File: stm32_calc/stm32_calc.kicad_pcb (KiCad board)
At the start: 2 copper layers, 76.2 x 132.2 mm, 83 parts, among them IC1 TM1638, J2 Conn_01x03, J3 C5307759, J4 Conn_02x03_Odd_Even, Q1 p channel mosfet sot 23, SW1 batter_switch, SW2 SS-1290, SW3 Reset, U1 STM32F072CBT6, U2 USBLC6-2SC6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

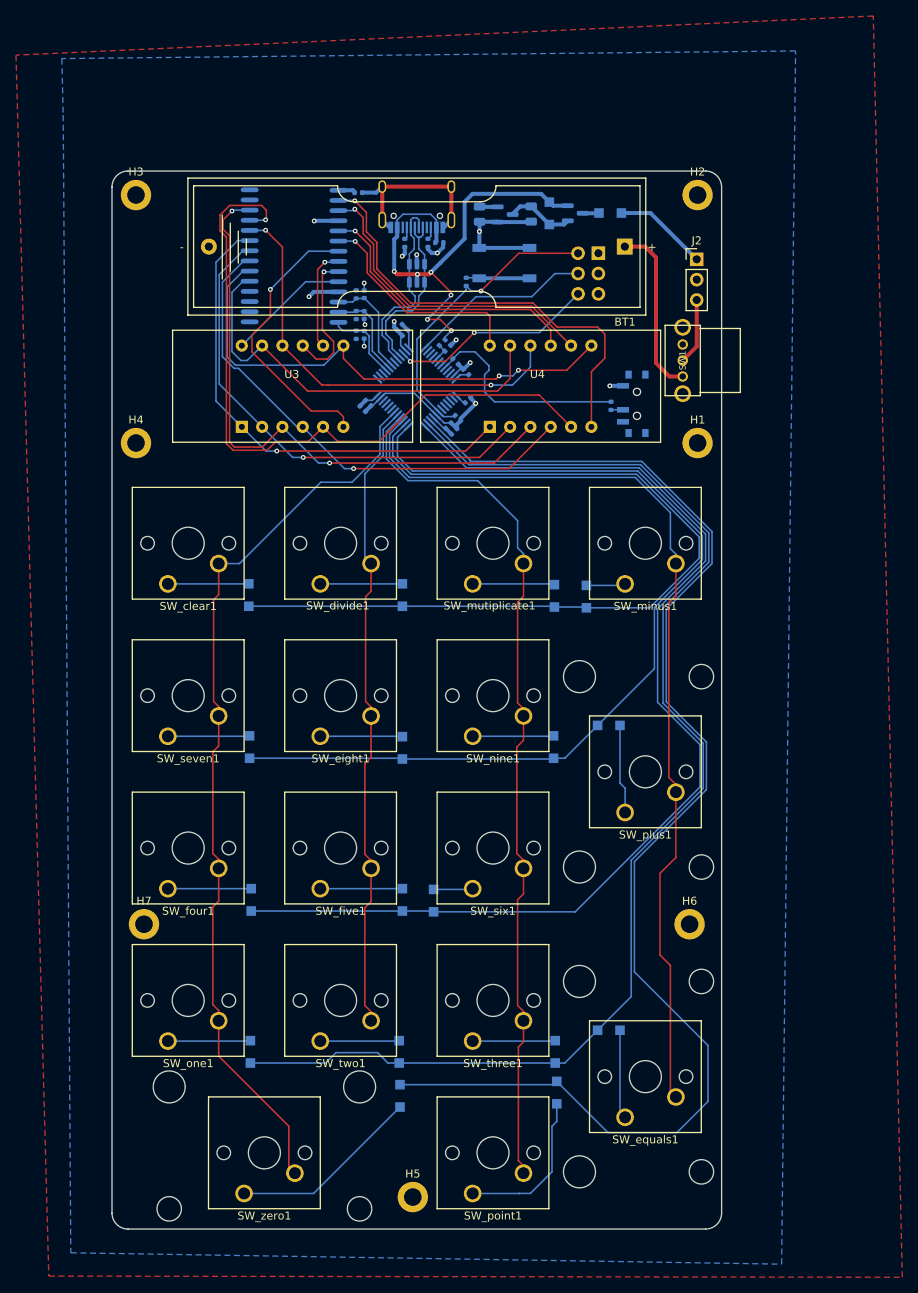
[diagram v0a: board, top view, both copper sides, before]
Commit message: added graphics, fixed some tracing
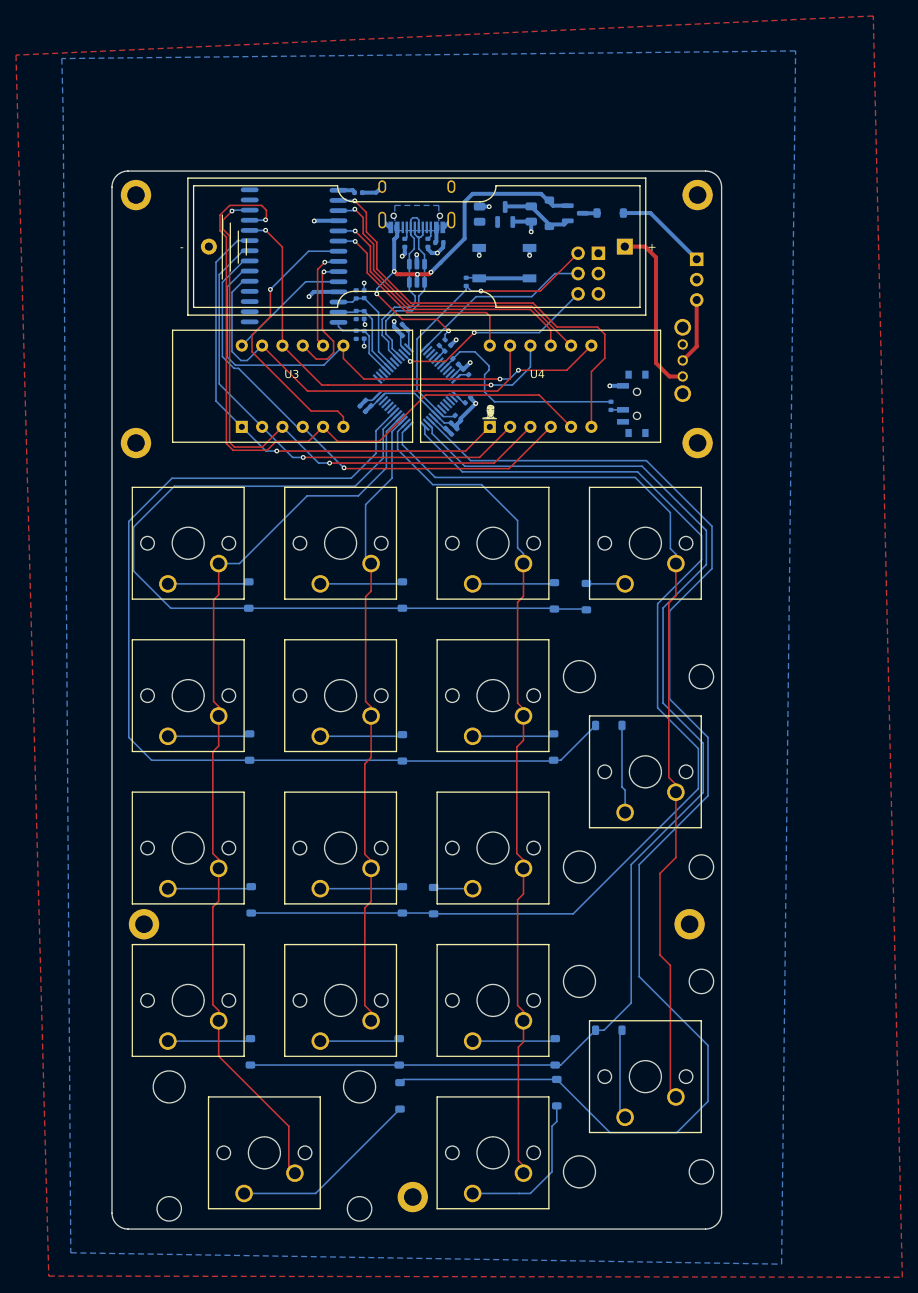
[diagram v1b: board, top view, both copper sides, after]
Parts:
- added G***: LOGO, georgs_lib:soy, F.Cu at (94.8, 88.2)
- added G***: LOGO, georgs_lib:math_signs, B.Cu at (81.9, 122.2)
- D1, D10, D11, D12, D13, D14, D15, D16, D17, D18, D19, D2, D3, D4, D5, D6, D7, D8, D9: footprint Diode_SMD:Nexperia_CFP3_SOD-123W -> Diode_SMD:D_SOD-123
- turned C20 to 90 degrees
- turned U5 to 90 degrees
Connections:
- U1 pad 13: row1 -> col3
- U1 pad 14: row0 -> col2
- U1 pad 15: col3 -> col1
- U1 pad 16: col2 -> col0
- U1 pad 17: col1 -> row0
- U1 pad 18: col0 -> row1
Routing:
- net GND: track 84.8 -> 58.4 mm, vias 14 -> 17
- net row1: track 121.0 -> 129.0 mm
- net vbus: track 58.9 -> 54.2 mm, vias 6 -> 5
- net col3: track 120.0 -> 116.3 mm
- net row0: track 108.9 -> 105.4 mm
- net col2: track 109.8 -> 106.7 mm
- net +3V3: track 17.0 -> 14.8 mm
- net col0: track 113.7 -> 114.8 mm
- net +5V: track 8.47 -> 8.98 mm
- added copper zone on B.Cu, net vbus
